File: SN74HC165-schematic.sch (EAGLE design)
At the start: 11 parts, among them U1 SN74HC165DR, U2 ESP-WROOM-32

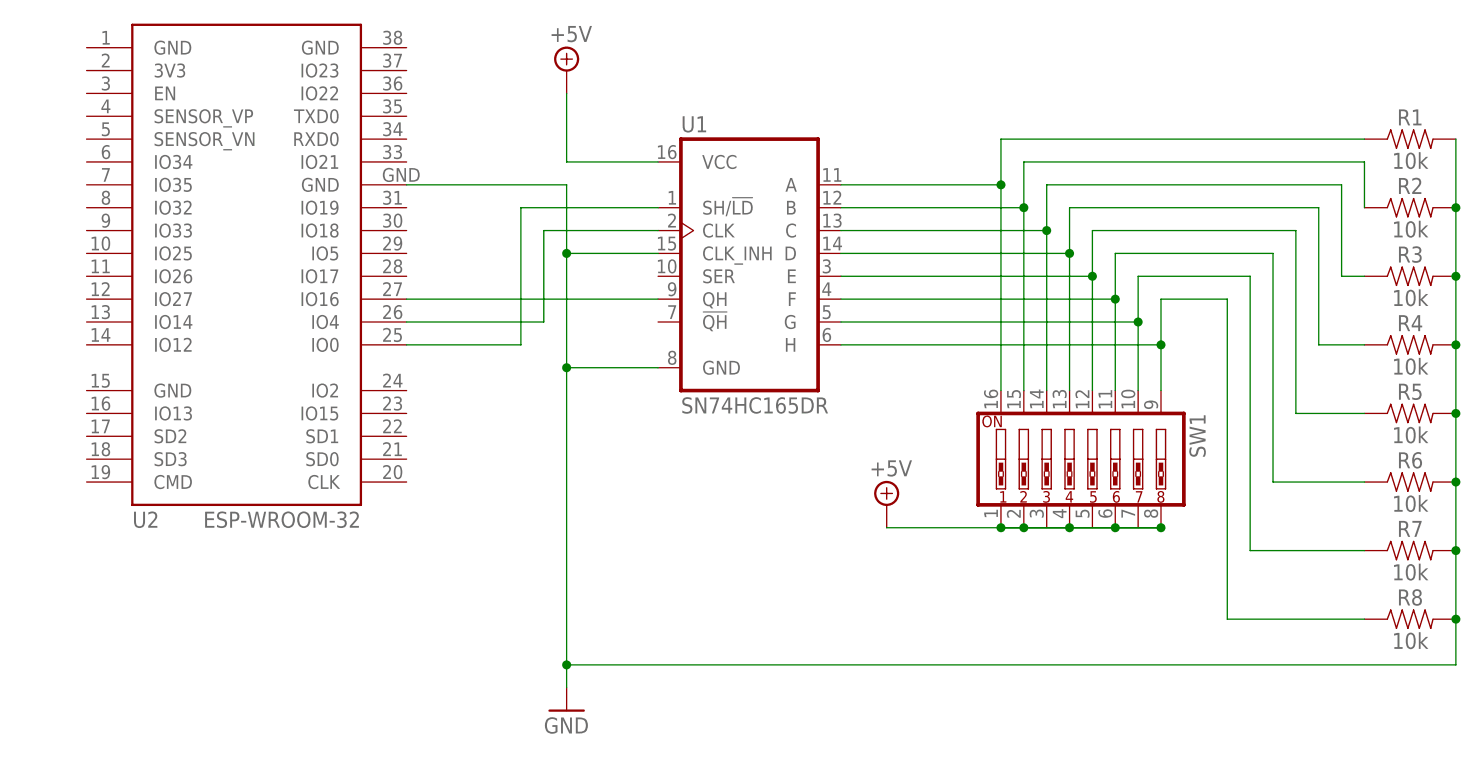
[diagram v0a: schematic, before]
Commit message: fixing connectivity diagram mistake
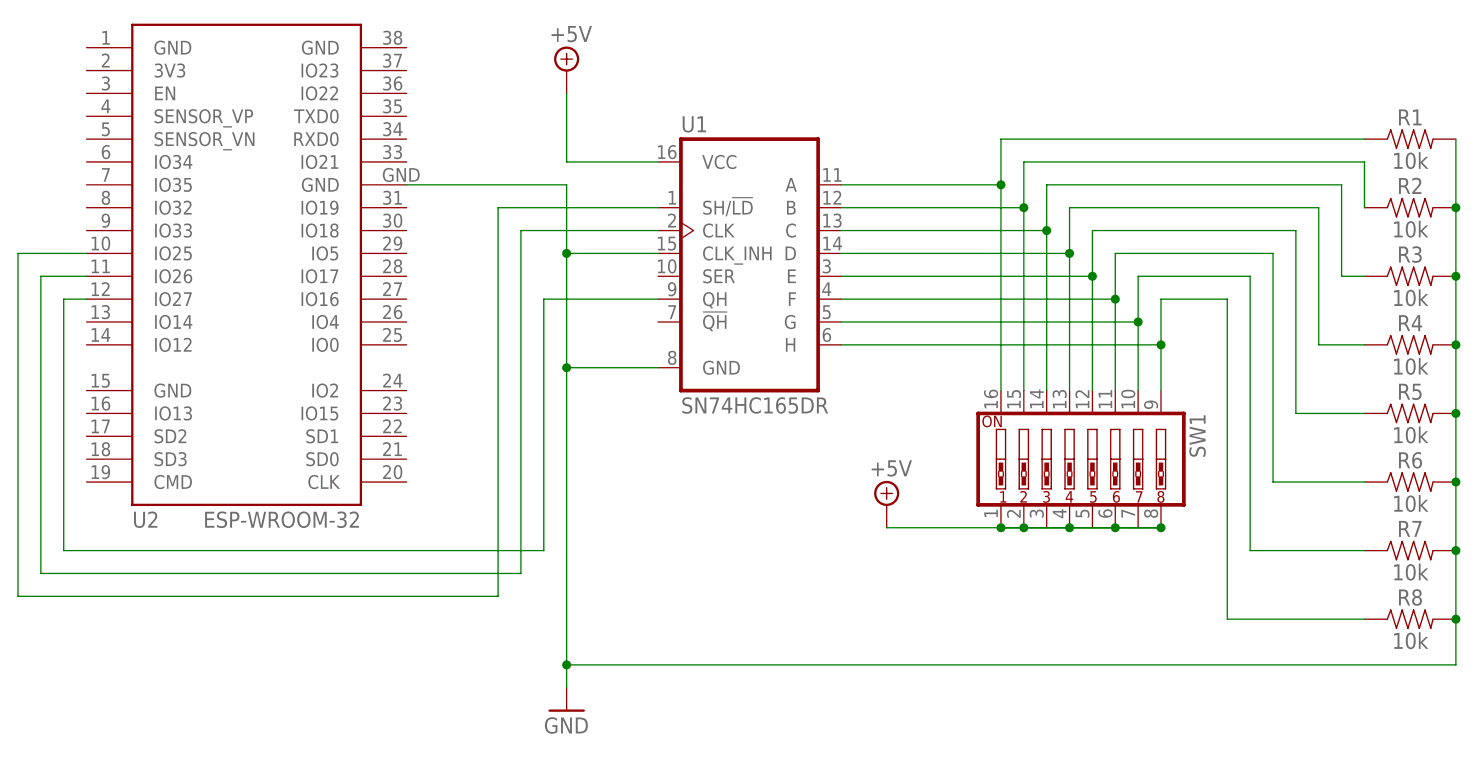
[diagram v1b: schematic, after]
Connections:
- net N$10: now also U2.IO26; no longer U2.IO4
- net N$11: now also U2.IO25; no longer U2.IO0
- net N$9: now also U2.IO27; no longer U2.IO16
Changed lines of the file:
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@@
-</segment>
-</net>
-<net name="N$9" class="0">
-<segment>
-<pinref part="U2" gate="G$1" pin="IO16"/>
-<pinref part="U1" gate="U1" pin="QH"/>
-<wire x1="-12.7" y1="86.36" x2="15.24" y2="86.36" width="0.1524" layer="91"/>
-</segment>
-</net>
-<net name="N$10" class="0">
-<segment>
-<pinref part="U2" gate="G$1" pin="IO4"/>
-<wire x1="-12.7" y1="83.82" x2="2.54" y2="83.82" width="0.1524" layer="91"/>
-<wire x1="2.54" y1="83.82" x2="2.54" y2="93.98" width="0.1524" layer="91"/>
-<pinref part="U1" gate="U1" pin="CLK"/>
-<wire x1="2.54" y1="93.98" x2="15.24" y2="93.98" width="0.1524" layer="91"/>
-</segment>
-</net>
-<net name="N$11" class="0">
-<segment>
-<pinref part="U2" gate="G$1" pin="IO0"/>
-<wire x1="-12.7" y1="81.28" x2="0" y2="81.28" width="0.1524" layer="91"/>
-<wire x1="0" y1="81.28" x2="0" y2="96.52" width="0.1524" layer="91"/>
-<pinref part="U1" gate="U1" pin="SH/!LD"/>
-<wire x1="0" y1="96.52" x2="15.24" y2="96.52" width="0.1524" layer="91"/>
 </segment>
 </net>
@@
 </segment>
 </net>
+<net name="N$9" class="0">
+<segment>
+<pinref part="U2" gate="G$1" pin="IO27"/>
+<wire x1="-48.26" y1="86.36" x2="-50.8" y2="86.36" width="0.1524" layer="91"/>
+<wire x1="-50.8" y1="86.36" x2="-50.8" y2="58.42" width="0.1524" layer="91"/>
+<wire x1="-50.8" y1="58.42" x2="2.54" y2="58.42" width="0.1524" layer="91"/>
+<pinref part="U1" gate="U1" pin="QH"/>
+<wire x1="2.54" y1="58.42" x2="2.54" y2="86.36" width="0.1524" layer="91"/>
+<wire x1="2.54" y1="86.36" x2="15.24" y2="86.36" width="0.1524" layer="91"/>
+</segment>
+</net>
+<net name="N$10" class="0">
+<segment>
+<pinref part="U2" gate="G$1" pin="IO26"/>
+<wire x1="-48.26" y1="88.9" x2="-53.34" y2="88.9" width="0.1524" layer="91"/>
+<wire x1="-53.34" y1="88.9" x2="-53.34" y2="55.88" width="0.1524" layer="91"/>
+<wire x1="-53.34" y1="55.88" x2="0" y2="55.88" width="0.1524" layer="91"/>
+<wire x1="0" y1="55.88" x2="0" y2="93.98" width="0.1524" layer="91"/>
+<pinref part="U1" gate="U1" pin="CLK"/>
+<wire x1="0" y1="93.98" x2="15.24" y2="93.98" width="0.1524" layer="91"/>
+</segment>
+</net>
+<net name="N$11" class="0">
+<segment>
+<pinref part="U2" gate="G$1" pin="IO25"/>
+<wire x1="-48.26" y1="91.44" x2="-55.88" y2="91.44" width="0.1524" layer="91"/>
+<wire x1="-55.88" y1="91.44" x2="-55.88" y2="53.34" width="0.1524" layer="91"/>
+<wire x1="-55.88" y1="53.34" x2="-2.54" y2="53.34" width="0.1524" layer="91"/>
+<wire x1="-2.54" y1="53.34" x2="-2.54" y2="96.52" width="0.1524" layer="91"/>
+<pinref part="U1" gate="U1" pin="SH/!LD"/>
+<wire x1="-2.54" y1="96.52" x2="15.24" y2="96.52" width="0.1524" layer="91"/>
+</segment>
+</net>
